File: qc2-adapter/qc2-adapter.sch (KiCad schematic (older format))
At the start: 34 parts, among them J1 USB_B, J2 en-, J3 en+, Q1 BC548, Q10 BC548, Q2 BC558, Q3 BC558, Q4 BC548, Q5 BC548, Q6 BC558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

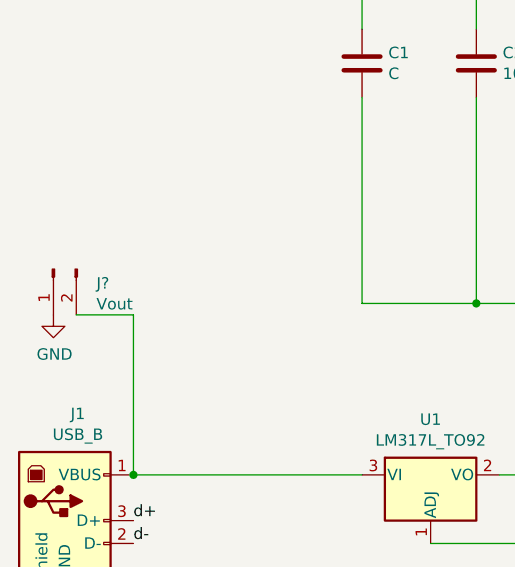
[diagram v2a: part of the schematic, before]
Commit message: qc2-adapter: add initial footprints
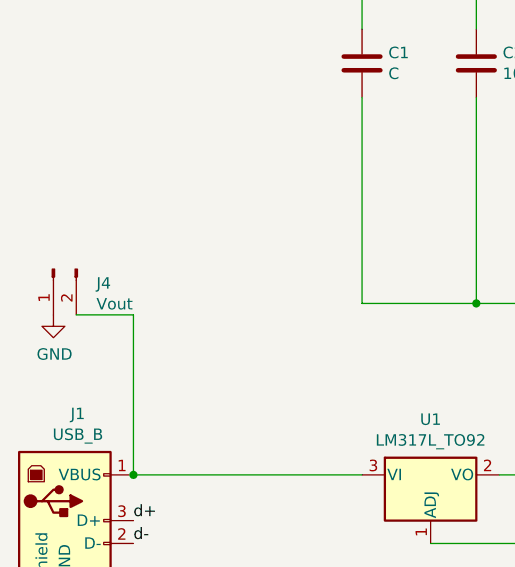
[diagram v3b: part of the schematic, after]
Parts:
- C1, C2, C3, C4, C5, C6: footprint (none) -> Capacitor_THT:C_Rect_L7.0mm_W2.0mm_P5.00mm
- J1: footprint (none) -> Connector_USB:USB_B_OST_USB-B1HSxx_Horizontal
- J2, J3: footprint (none) -> Connector_PinHeader_2.54mm:PinHeader_1x02_P2.54mm_Vertical
- J4: renamed from J?; footprint (none) -> Connector_PinHeader_2.54mm:PinHeader_1x02_P2.54mm_Vertical
- Q1, Q10, Q2, Q3, Q4, Q5, Q6, Q7, Q8, Q9, U1: footprint Package_TO_SOT_THT:TO-92_Inline -> Package_TO_SOT_THT:TO-92_Inline_Wide
- R1, R10, R11, R12, R2, R3, R4, R5, R6, R7, R8, R9: footprint (none) -> Resistor_THT:R_Axial_DIN0204_L3.6mm_D1.6mm_P2.54mm_Vertical
- U2: footprint (none) -> Package_DIP:DIP-8_W7.62mm_LongPads
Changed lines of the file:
@@
 F 0 "U2" H 4050 3731 50  0000 C CNN
 F 1 "LM555" H 4050 3640 50  0000 C CNN
-F 2 "" H 4050 3150 50  0001 C CNN
+F 2 "Package_DIP:DIP-8_W7.62mm_LongPads" H 4050 3150 50  0001 C CNN
 F 3 "http://www.ti.com/lit/ds/symlink/lm555.pdf" H 4050 3150 50  0001 C CNN
 	1    4050 3150
@@
 F 0 "R10" H 8320 1996 50  0000 L CNN
 F 1 "10k" H 8320 1905 50  0000 L CNN
-F 2 "" V 8180 1950 50  0001 C CNN
+F 2 "Resistor_THT:R_Axial_DIN0204_L3.6mm_D1.6mm_P2.54mm_Vertical" V 8180 1950 50  0001 C CNN
 F 3 "~" H 8250 1950 50  0001 C CNN
 	1    8250 1950
@@
 F 0 "Q10" H 9941 4296 50  0000 L CNN
 F 1 "BC548" H 9941 4205 50  0000 L CNN
-F 2 "Package_TO_SOT_THT:TO-92_Inline" H 9950 4175 50  0001 L CIN
+F 2 "Package_TO_SOT_THT:TO-92_Inline_Wide" H 9950 4175 50  0001 L CIN
 F 3 "http://www.fairchildsemi.com/ds/BC/BC547.pdf" H 9750 4250 50  0001 L CNN
 	1    9750 4250
@@
 F 0 "Q4" H 7591 4496 50  0000 L CNN
 F 1 "BC548" H 7591 4405 50  0000 L CNN
-F 2 "Package_TO_SOT_THT:TO-92_Inline" H 7600 4375 50  0001 L CIN
+F 2 "Package_TO_SOT_THT:TO-92_Inline_Wide" H 7600 4375 50  0001 L CIN
 F 3 "http://www.fairchildsemi.com/ds/BC/BC547.pdf" H 7400 4450 50  0001 L CNN
 	1    7400 4450
@@
 F 0 "Q5" H 8241 4496 50  0000 L CNN
 F 1 "BC548" H 8241 4405 50  0000 L CNN
-F 2 "Package_TO_SOT_THT:TO-92_Inline" H 8250 4375 50  0001 L CIN
+F 2 "Package_TO_SOT_THT:TO-92_Inline_Wide" H 8250 4375 50  0001 L CIN
 F 3 "http://www.fairchildsemi.com/ds/BC/BC547.pdf" H 8050 4450 50  0001 L CNN
 	1    8050 4450
@@
 F 0 "R11" H 8670 3196 50  0000 L CNN
 F 1 "10k" H 8670 3105 50  0000 L CNN
-F 2 "" V 8530 3150 50  0001 C CNN
+F 2 "Resistor_THT:R_Axial_DIN0204_L3.6mm_D1.6mm_P2.54mm_Vertical" V 8530 3150 50  0001 C CNN
 F 3 "~" H 8600 3150 50  0001 C CNN
 	1    8600 3150
@@
 F 0 "C6" H 9615 4496 50  0000 L CNN
 F 1 "C" H 9615 4405 50  0000 L CNN
-F 2 "" H 9538 4300 50  0001 C CNN
+F 2 "Capacitor_THT:C_Rect_L7.0mm_W2.0mm_P5.00mm" H 9538 4300 50  0001 C CNN
 F 3 "~" H 9500 4450 50  0001 C CNN
 	1    9500 4450
@@
 F 0 "C5" H 9615 3196 50  0000 L CNN
 F 1 "C" H 9615 3105 50  0000 L CNN
-F 2 "" H 9538 3000 50  0001 C CNN
+F 2 "Capacitor_THT:C_Rect_L7.0mm_W2.0mm_P5.00mm" H 9538 3000 50  0001 C CNN
 F 3 "~" H 9500 3150 50  0001 C CNN
 	1    9500 3150
@@
 F 0 "R12" H 8870 4496 50  0000 L CNN
 F 1 "10k" H 8870 4405 50  0000 L CNN
-F 2 "" V 8730 4450 50  0001 C CNN
+F 2 "Resistor_THT:R_Axial_DIN0204_L3.6mm_D1.6mm_P2.54mm_Vertical" V 8730 4450 50  0001 C CNN
 F 3 "~" H 8800 4450 50  0001 C CNN
 	1    8800 4450
@@
 F 0 "Q1" H 6391 4496 50  0000 L CNN
 F 1 "BC548" H 6391 4405 50  0000 L CNN
-F 2 "Package_TO_SOT_THT:TO-92_Inline" H 6400 4375 50  0001 L CIN
+F 2 "Package_TO_SOT_THT:TO-92_Inline_Wide" H 6400 4375 50  0001 L CIN
 F 3 "http://www.fairchildsemi.com/ds/BC/BC547.pdf" H 6200 4450 50  0001 L CNN
 	1    6200 4450
@@
 F 0 "R7" H 6370 1596 50  0000 L CNN
 F 1 "10k" H 6370 1505 50  0000 L CNN
-F 2 "" V 6230 1550 50  0001 C CNN
+F 2 "Resistor_THT:R_Axial_DIN0204_L3.6mm_D1.6mm_P2.54mm_Vertical" V 6230 1550 50  0001 C CNN
 F 3 "~" H 6300 1550 50  0001 C CNN
 	1    6300 1550
@@
 F 0 "R6" V 5193 2950 50  0000 C CNN
 F 1 "4.7k" V 5284 2950 50  0000 C CNN
-F 2 "" V 5330 2950 50  0001 C CNN
+F 2 "Resistor_THT:R_Axial_DIN0204_L3.6mm_D1.6mm_P2.54mm_Vertical" V 5330 2950 50  0001 C CNN
 F 3 "~" H 5400 2950 50  0001 C CNN
 	1    5400 2950
@@
 F 0 "C4" H 4965 3646 50  0000 L CNN
 F 1 "150nF" H 4965 3555 50  0000 L CNN
-F 2 "" H 4888 3450 50  0001 C CNN
+F 2 "Capacitor_THT:C_Rect_L7.0mm_W2.0mm_P5.00mm" H 4888 3450 50  0001 C CNN
 F 3 "~" H 4850 3600 50  0001 C CNN
 	1    4850 3600
@@
 F 0 "R5" H 4920 2346 50  0000 L CNN
 F 1 "10k" H 4920 2255 50  0000 L CNN
-F 2 "" V 4780 2300 50  0001 C CNN
+F 2 "Resistor_THT:R_Axial_DIN0204_L3.6mm_D1.6mm_P2.54mm_Vertical" V 4780 2300 50  0001 C CNN
 F 3 "~" H 4850 2300 50  0001 C CNN
 	1    4850 2300
@@
 F 0 "C2" H 3265 3646 50  0000 L CNN
 F 1 "10nF" H 3265 3555 50  0000 L CNN
-F 2 "" H 3188 3450 50  0001 C CNN
+F 2 "Capacitor_THT:C_Rect_L7.0mm_W2.0mm_P5.00mm" H 3188 3450 50  0001 C CNN
 F 3 "~" H 3150 3600 50  0001 C CNN
 	1    3150 3600
@@
 F 0 "C1" H 2765 3646 50  0000 L CNN
 F 1 "C" H 2765 3555 50  0000 L CNN
-F 2 "" H 2688 3450 50  0001 C CNN
+F 2 "Capacitor_THT:C_Rect_L7.0mm_W2.0mm_P5.00mm" H 2688 3450 50  0001 C CNN
 F 3 "~" H 2650 3600 50  0001 C CNN
 	1    2650 3600
@@
 F 0 "R1" H 2720 2346 50  0000 L CNN
 F 1 "R" H 2720 2255 50  0000 L CNN
-F 2 "" V 2580 2300 50  0001 C CNN
+F 2 "Resistor_THT:R_Axial_DIN0204_L3.6mm_D1.6mm_P2.54mm_Vertical" V 2580 2300 50  0001 C CNN
 F 3 "~" H 2650 2300 50  0001 C CNN
 	1    2650 2300
@@
 F 0 "Q2" H 7591 846 50  0000 L CNN
 F 1 "BC558" H 7591 755 50  0000 L CNN
-F 2 "Package_TO_SOT_THT:TO-92_Inline" H 7600 725 50  0001 L CIN
+F 2 "Package_TO_SOT_THT:TO-92_Inline_Wide" H 7600 725 50  0001 L CIN
 F 3 "http://www.fairchildsemi.com/ds/BC/BC557.pdf" H 7400 800 50  0001 L CNN
 	1    7400 800
@@
 F 0 "Q7" H 8341 2996 50  0000 L CNN
 F 1 "BC558" H 8341 2905 50  0000 L CNN
-F 2 "Package_TO_SOT_THT:TO-92_Inline" H 8350 2875 50  0001 L CIN
+F 2 "Package_TO_SOT_THT:TO-92_Inline_Wide" H 8350 2875 50  0001 L CIN
 F 3 "http://www.fairchildsemi.com/ds/BC/BC557.pdf" H 8150 2950 50  0001 L CNN
 	1    8150 2950
@@
 F 0 "Q3" H 7591 2996 50  0000 L CNN
 F 1 "BC558" H 7591 2905 50  0000 L CNN
-F 2 "Package_TO_SOT_THT:TO-92_Inline" H 7600 2875 50  0001 L CIN
+F 2 "Package_TO_SOT_THT:TO-92_Inline_Wide" H 7600 2875 50  0001 L CIN
 F 3 "http://www.fairchildsemi.com/ds/BC/BC557.pdf" H 7400 2950 50  0001 L CNN
 	1    7400 2950
@@
 F 0 "Q9" H 9941 3696 50  0000 L CNN
 F 1 "BC558" H 9941 3605 50  0000 L CNN
-F 2 "Package_TO_SOT_THT:TO-92_Inline" H 9950 3575 50  0001 L CIN
+F 2 "Package_TO_SOT_THT:TO-92_Inline_Wide" H 9950 3575 50  0001 L CIN
 F 3 "http://www.fairchildsemi.com/ds/BC/BC557.pdf" H 9750 3650 50  0001 L CNN
 	1    9750 3650
@@
 F 0 "Q8" H 9941 1546 50  0000 L CNN
 F 1 "BC558" H 9941 1455 50  0000 L CNN
-F 2 "Package_TO_SOT_THT:TO-92_Inline" H 9950 1425 50  0001 L CIN
+F 2 "Package_TO_SOT_THT:TO-92_Inline_Wide" H 9950 1425 50  0001 L CIN
 F 3 "http://www.fairchildsemi.com/ds/BC/BC557.pdf" H 9750 1500 50  0001 L CNN
 	1    9750 1500
@@
 F 0 "Q6" H 8341 846 50  0000 L CNN
 F 1 "BC558" H 8341 755 50  0000 L CNN
-F 2 "Package_TO_SOT_THT:TO-92_Inline" H 8350 725 50  0001 L CIN
+F 2 "Package_TO_SOT_THT:TO-92_Inline_Wide" H 8350 725 50  0001 L CIN
 F 3 "http://www.fairchildsemi.com/ds/BC/BC557.pdf" H 8150 800 50  0001 L CNN
 	1    8150 800
@@
 F 0 "J2" V 7212 3344 50  0000 L CNN
 F 1 "en-" V 7303 3344 50  0000 L CNN
-F 2 "" H 7150 3300 50  0001 C CNN
+F 2 "Connector_PinHeader_2.54mm:PinHeader_1x02_P2.54mm_Vertical" H 7150 3300 50  0001 C CNN
 F 3 "~" H 7150 3300 50  0001 C CNN
 	1    7150 3300
@@
 F 0 "J3" V 7712 1494 50  0000 L CNN
 F 1 "en+" V 7803 1494 50  0000 L CNN
-F 2 "" H 7650 1450 50  0001 C CNN
+F 2 "Connector_PinHeader_2.54mm:PinHeader_1x02_P2.54mm_Vertical" H 7650 1450 50  0001 C CNN
 F 3 "~" H 7650 1450 50  0001 C CNN
 	1    7650 1450
@@
 F 0 "R9" H 7620 1996 50  0000 L CNN
 F 1 "10k" H 7620 1905 50  0000 L CNN
-F 2 "" V 7480 1950 50  0001 C CNN
+F 2 "Resistor_THT:R_Axial_DIN0204_L3.6mm_D1.6mm_P2.54mm_Vertical" V 7480 1950 50  0001 C CNN
 F 3 "~" H 7550 1950 50  0001 C CNN
 	1    7550 1950
@@
 F 0 "R8" V 7093 3950 50  0000 C CNN
 F 1 "4.7k" V 7184 3950 50  0000 C CNN
-F 2 "" V 7230 3950 50  0001 C CNN
+F 2 "Resistor_THT:R_Axial_DIN0204_L3.6mm_D1.6mm_P2.54mm_Vertical" V 7230 3950 50  0001 C CNN
 F 3 "~" H 7300 3950 50  0001 C CNN
 	1    7300 3950
@@
 F 0 "U1" H 2950 5642 50  0000 C CNN
 F 1 "LM317L_TO92" H 2950 5551 50  0000 C CNN
-F 2 "Package_TO_SOT_THT:TO-92_Inline" H 2950 5625 50  0001 C CIN
+F 2 "Package_TO_SOT_THT:TO-92_Inline_Wide" H 2950 5625 50  0001 C CIN
 F 3 "http://www.ti.com/lit/ds/snvs775k/snvs775k.pdf" H 2950 5400 50  0001 C CNN
 	1    2950 5400
@@
 F 0 "R2" H 3470 5596 50  0000 L CNN
 F 1 "220" H 3470 5505 50  0000 L CNN
-F 2 "" V 3330 5550 50  0001 C CNN
+F 2 "Resistor_THT:R_Axial_DIN0204_L3.6mm_D1.6mm_P2.54mm_Vertical" V 3330 5550 50  0001 C CNN
 F 3 "~" H 3400 5550 50  0001 C CNN
 	1    3400 5550
@@
 F 0 "R3" H 3470 5996 50  0000 L CNN
 F 1 "330" H 3470 5905 50  0000 L CNN
-F 2 "" V 3330 5950 50  0001 C CNN
+F 2 "Resistor_THT:R_Axial_DIN0204_L3.6mm_D1.6mm_P2.54mm_Vertical" V 3330 5950 50  0001 C CNN
 F 3 "~" H 3400 5950 50  0001 C CNN
 	1    3400 5950
@@
 F 0 "R4" H 3470 6396 50  0000 L CNN
 F 1 "330" H 3470 6305 50  0000 L CNN
-F 2 "" V 3330 6350 50  0001 C CNN
+F 2 "Resistor_THT:R_Axial_DIN0204_L3.6mm_D1.6mm_P2.54mm_Vertical" V 3330 6350 50  0001 C CNN
 F 3 "~" H 3400 6350 50  0001 C CNN
 	1    3400 6350
@@
 F 0 "C3" H 4115 5996 50  0000 L CNN
 F 1 "C" H 4115 5905 50  0000 L CNN
-F 2 "" H 4038 5800 50  0001 C CNN
+F 2 "Capacitor_THT:C_Rect_L7.0mm_W2.0mm_P5.00mm" H 4038 5800 50  0001 C CNN
 F 3 "~" H 4000 5950 50  0001 C CNN
 	1    4000 5950
@@
 F 0 "J1" H 1407 6067 50  0000 C CNN
 F 1 "USB_B" H 1407 5976 50  0000 C CNN
-F 2 "" H 1500 5550 50  0001 C CNN
+F 2 "Connector_USB:USB_B_OST_USB-B1HSxx_Horizontal" H 1500 5550 50  0001 C CNN
 F 3 " ~" H 1500 5550 50  0001 C CNN
 	1    1350 5600
@@
 Connection ~ 1350 6000
 $Comp
-L Connector:Conn_01x02_Male J?
+L Connector:Conn_01x02_Male J4
 U 1 1 5E0B7E4E
 P 1300 4500
-F 0 "J?" V 1362 4312 50  0000 R CNN
+F 0 "J4" V 1362 4312 50  0000 R CNN
 F 1 "Vout" V 1453 4312 50  0000 R CNN
-F 2 "" H 1300 4500 50  0001 C CNN
+F 2 "Connector_PinHeader_2.54mm:PinHeader_1x02_P2.54mm_Vertical" H 1300 4500 50  0001 C CNN
 F 3 "~" H 1300 4500 50  0001 C CNN
 	1    1300 4500
@@
 $EndComp
 $Comp
-L power:GND #PWR?
+L power:GND #PWR0107
 U 1 1 5E0C363B
 P 1300 4700
-F 0 "#PWR?" H 1300 4450 50  0001 C CNN
+F 0 "#PWR0107" H 1300 4450 50  0001 C CNN
 F 1 "GND" H 1305 4527 50  0000 C CNN
 F 2 "" H 1300 4700 50  0001 C CNN

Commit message: qc2-adapter: fix only schem/netlist: add voltage dividers
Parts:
- added R13, R16: 10k, Resistor_THT:R_Axial_DIN0204_L3.6mm_D1.6mm_P2.54mm_Vertical, symbol Device:R
- added R14, R17: 1.5k, Resistor_THT:R_Axial_DIN0204_L3.6mm_D1.6mm_P2.54mm_Vertical, symbol Device:R
- added R15, R18: 470, Resistor_THT:R_Axial_DIN0204_L3.6mm_D1.6mm_P2.54mm_Vertical, symbol Device:R
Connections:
- net +5V: now also R13.1, R16.1
- net GND: now also R14.2, R17.2
- net d+: now also R13.2, R14.1, R15.2; no longer Q8.1 (C)
- net d-: now also R16.2, R17.1, R18.2; no longer Q10.1 (C), Q9.1 (C)
- new net d+control: Q8.1 (C), R15.1
- new net d-control: Q10.1 (C), Q9.1 (C), R18.1
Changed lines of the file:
@@
 Wire Wire Line
 	7200 800  6750 800
-Text Label 9850 1800 0    50   ~ 0
+Text Label 5200 5700 0    50   ~ 0
 d+
 $Comp
@@
 	7550 2100 7550 2500
 Connection ~ 7550 2500
-Text Label 9850 3950 0    50   ~ 0
+Text Label 6250 5700 0    50   ~ 0
 d-
 $Comp
@@
 Text Label 4200 4650 0    50   ~ 0
 GND
+$Comp
+L Device:R R13
+U 1 1 5E0DB67F
+P 5200 5450
+F 0 "R13" H 5270 5496 50  0000 L CNN
+F 1 "10k" H 5270 5405 50  0000 L CNN
+F 2 "Resistor_THT:R_Axial_DIN0204_L3.6mm_D1.6mm_P2.54mm_Vertical" V 5130 5450 50  0001 C CNN
+F 3 "~" H 5200 5450 50  0001 C CNN
+	1    5200 5450
+	1    0    0    -1
+$EndComp
+$Comp
+L Device:R R14
+U 1 1 5E0DBDBA
+P 5200 5950
+F 0 "R14" H 5270 5996 50  0000 L CNN
+F 1 "1.5k" H 5270 5905 50  0000 L CNN
+F 2 "Resistor_THT:R_Axial_DIN0204_L3.6mm_D1.6mm_P2.54mm_Vertical" V 5130 5950 50  0001 C CNN
+F 3 "~" H 5200 5950 50  0001 C CNN
+	1    5200 5950
+	1    0    0    -1
+$EndComp
+$Comp
+L Device:R R16
+U 1 1 5E0DC6DD
+P 6250 5450
+F 0 "R16" H 6320 5496 50  0000 L CNN
+F 1 "10k" H 6320 5405 50  0000 L CNN
+F 2 "Resistor_THT:R_Axial_DIN0204_L3.6mm_D1.6mm_P2.54mm_Vertical" V 6180 5450 50  0001 C CNN
+F 3 "~" H 6250 5450 50  0001 C CNN
+	1    6250 5450
+	1    0    0    -1
+$EndComp
+$Comp
+L Device:R R17
+U 1 1 5E0DC6E7
+P 6250 5950
+F 0 "R17" H 6320 5996 50  0000 L CNN
+F 1 "1.5k" H 6320 5905 50  0000 L CNN
+F 2 "Resistor_THT:R_Axial_DIN0204_L3.6mm_D1.6mm_P2.54mm_Vertical" V 6180 5950 50  0001 C CNN
+F 3 "~" H 6250 5950 50  0001 C CNN
+	1    6250 5950
+	1    0    0    -1
+$EndComp
+$Comp
+L Device:R R15
+U 1 1 5E0E0A0A
+P 5600 5700
+F 0 "R15" V 5393 5700 50  0000 C CNN
+F 1 "470" V 5484 5700 50  0000 C CNN
+F 2 "Resistor_THT:R_Axial_DIN0204_L3.6mm_D1.6mm_P2.54mm_Vertical" V 5530 5700 50  0001 C CNN
+F 3 "~" H 5600 5700 50  0001 C CNN
+	1    5600 5700
+	0    1    1    0
+$EndComp
+$Comp
+L Device:R R18
+U 1 1 5E0E53E4
+P 6650 5700
+F 0 "R18" V 6443 5700 50  0000 C CNN
+F 1 "470" V 6534 5700 50  0000 C CNN
+F 2 "Resistor_THT:R_Axial_DIN0204_L3.6mm_D1.6mm_P2.54mm_Vertical" V 6580 5700 50  0001 C CNN
+F 3 "~" H 6650 5700 50  0001 C CNN
+	1    6650 5700
+	0    1    1    0
+$EndComp
+Wire Wire Line
+	5200 5600 5200 5700
+Wire Wire Line
+	5450 5700 5200 5700
+Connection ~ 5200 5700
+Wire Wire Line
+	5200 5700 5200 5800
+Wire Wire Line
+	6250 5600 6250 5700
+Wire Wire Line
+	6500 5700 6250 5700
+Connection ~ 6250 5700
+Wire Wire Line
+	6250 5700 6250 5800
+Wire Wire Line
+	6250 6100 5200 6100
+$Comp
+L power:GND #PWR02
+U 1 1 5E0FAB4B
+P 5200 6100
+F 0 "#PWR02" H 5200 5850 50  0001 C CNN
+F 1 "GND" H 5205 5927 50  0000 C CNN
+F 2 "" H 5200 6100 50  0001 C CNN
+F 3 "" H 5200 6100 50  0001 C CNN
+	1    5200 6100
+	1    0    0    -1
+$EndComp
+Connection ~ 5200 6100
+$Comp
+L power:+5V #PWR01
+U 1 1 5E0FAE4D
+P 5200 5300
+F 0 "#PWR01" H 5200 5150 50  0001 C CNN
+F 1 "+5V" H 5215 5473 50  0000 C CNN
+F 2 "" H 5200 5300 50  0001 C CNN
+F 3 "" H 5200 5300 50  0001 C CNN
+	1    5200 5300
+	1    0    0    -1
+$EndComp
+Wire Wire Line
+	6250 5300 5200 5300
+Connection ~ 5200 5300
+Text Label 9850 3950 0    50   ~ 0
+d-control
+Text Label 6800 5700 0    50   ~ 0
+d-control
+Text Label 5750 5700 0    50   ~ 0
+d+control
+Text Label 9850 1900 0    50   ~ 0
+d+control
 $EndSCHEMATC
